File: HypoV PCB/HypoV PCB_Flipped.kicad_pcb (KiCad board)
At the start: 2 copper layers, 61.5 x 43 mm, 12 parts, among them J1 Conn_Header_JST_PH_1x02_P2mm_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

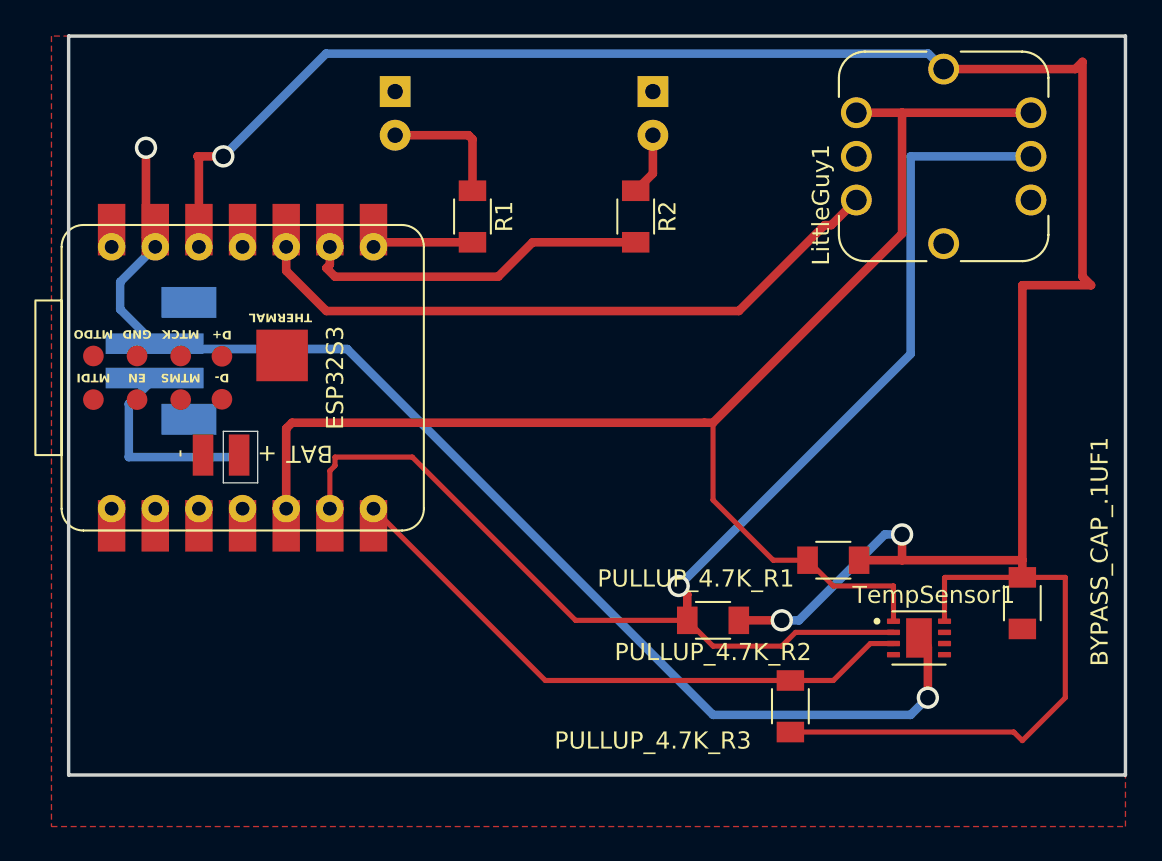
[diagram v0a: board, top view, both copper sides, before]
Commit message: added the breakout board
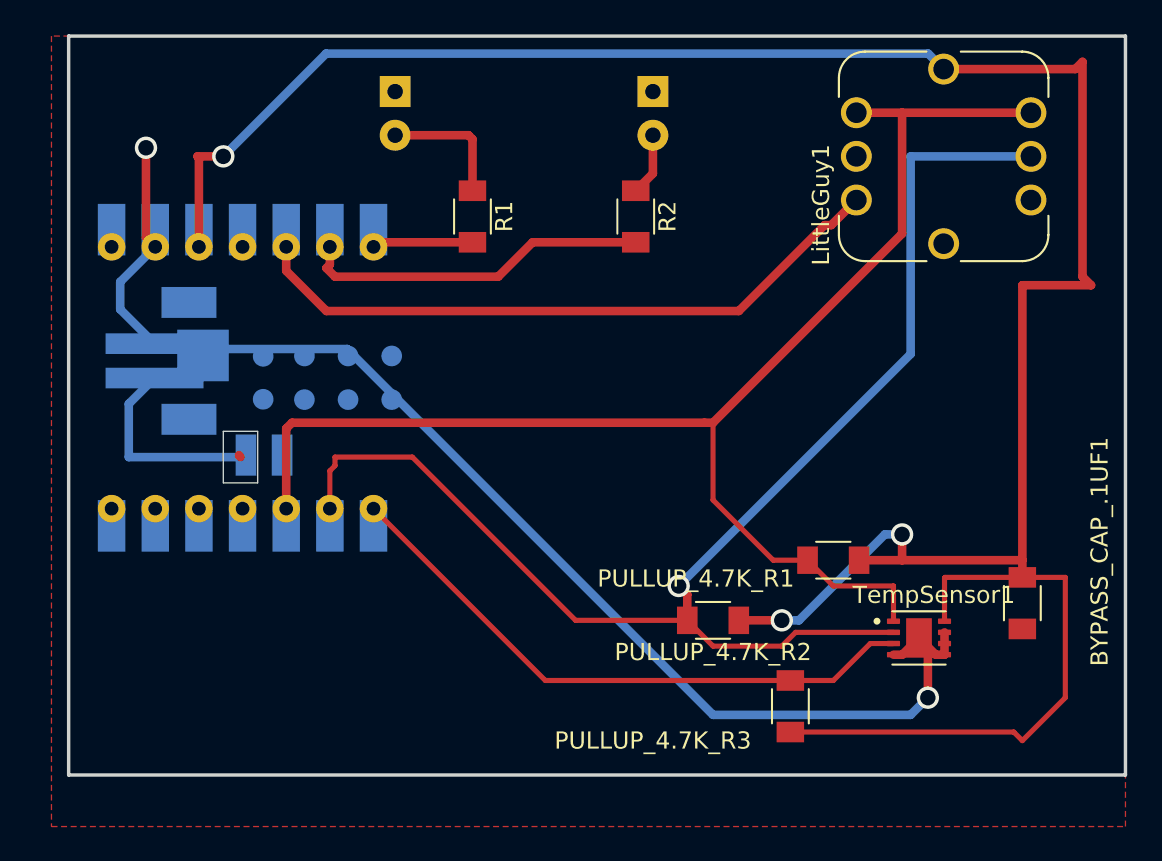
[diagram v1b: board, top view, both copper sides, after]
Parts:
- ESP32S3: moved to B.Cu
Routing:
- net GND: track 69.0 -> 74.1 mm
